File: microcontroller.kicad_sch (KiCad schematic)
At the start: 1 part, among them U1 STM32H745XIH6

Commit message: add power path sheet
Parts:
- U1: LCSC (none) -> C1338373
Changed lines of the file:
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@@
+			)
+		)
+		(property "LCSC" "C1338373"
+			(at 200.66 52.07 0)
+			(hide yes)
+			(show_name no)
+			(do_not_autoplace no)
+			(effects
+				(font
+					(size 1.27 1.27)
+				)
 			)
 		)
@@
 			)
 		)
+		(property "LCSC" "C1338373"
+			(at 59.69 100.33 0)
+			(hide yes)
+			(show_name no)
+			(do_not_autoplace no)
+			(effects
+				(font
+					(size 1.27 1.27)
+				)
+			)
+		)
 		(pin "D7"
 		)
@@
 			)
 		)
+		(property "LCSC" "C1338373"
+			(at 135.89 85.09 0)
+			(hide yes)
+			(show_name no)
+			(do_not_autoplace no)
+			(effects
+				(font
+					(size 1.27 1.27)
+				)
+			)
+		)

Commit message: fixed microcontroller footprint
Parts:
- U1: footprint STM32H745XIH6:BGA265C80P17X17_1400X1400X120 -> footprints:BGA265C80P17X17_1400X1400X120
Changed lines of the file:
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@@
 			)
 		)
-		(property "Footprint" "STM32H745XIH6:BGA265C80P17X17_1400X1400X120"
+		(property "Footprint" "footprints:BGA265C80P17X17_1400X1400X120"
 			(at 200.66 52.07 0)
 			(hide yes)
@@
 			)
 		)
-		(property "Footprint" "STM32H745XIH6:BGA265C80P17X17_1400X1400X120"
+		(property "Footprint" "footprints:BGA265C80P17X17_1400X1400X120"
 			(at 59.69 100.33 0)
 			(hide yes)
@@
 			)
 		)
-		(property "Footprint" "STM32H745XIH6:BGA265C80P17X17_1400X1400X120"
+		(property "Footprint" "footprints:BGA265C80P17X17_1400X1400X120"
 			(at 135.89 85.09 0)
 			(hide yes)

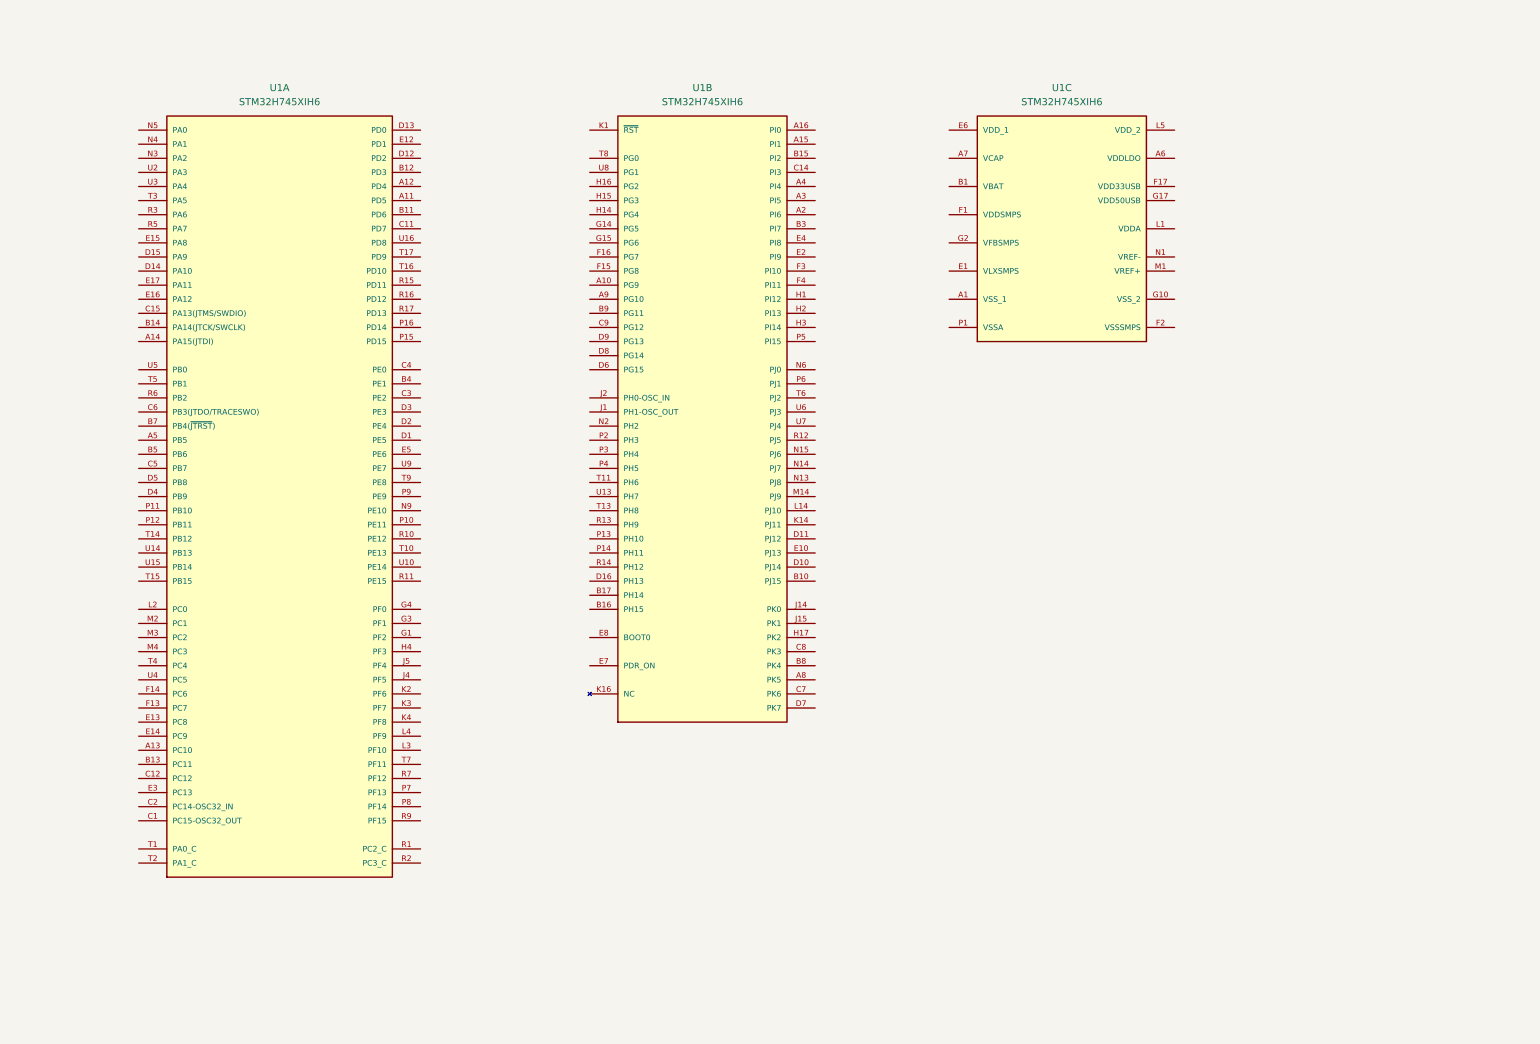
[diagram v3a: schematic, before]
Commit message: MCU (#2)
* add pedal cubemx file

* add microcontroller decoupling

* add decoupling caps

* fix footprints and add smps

* add user led

* add usb

* add debug pins

* add fmc pins, stomp uart, fuel gauge i2c

* update ioc

* add a bunch of peripherals

* add all external signals

* add no connects

* add oscillator
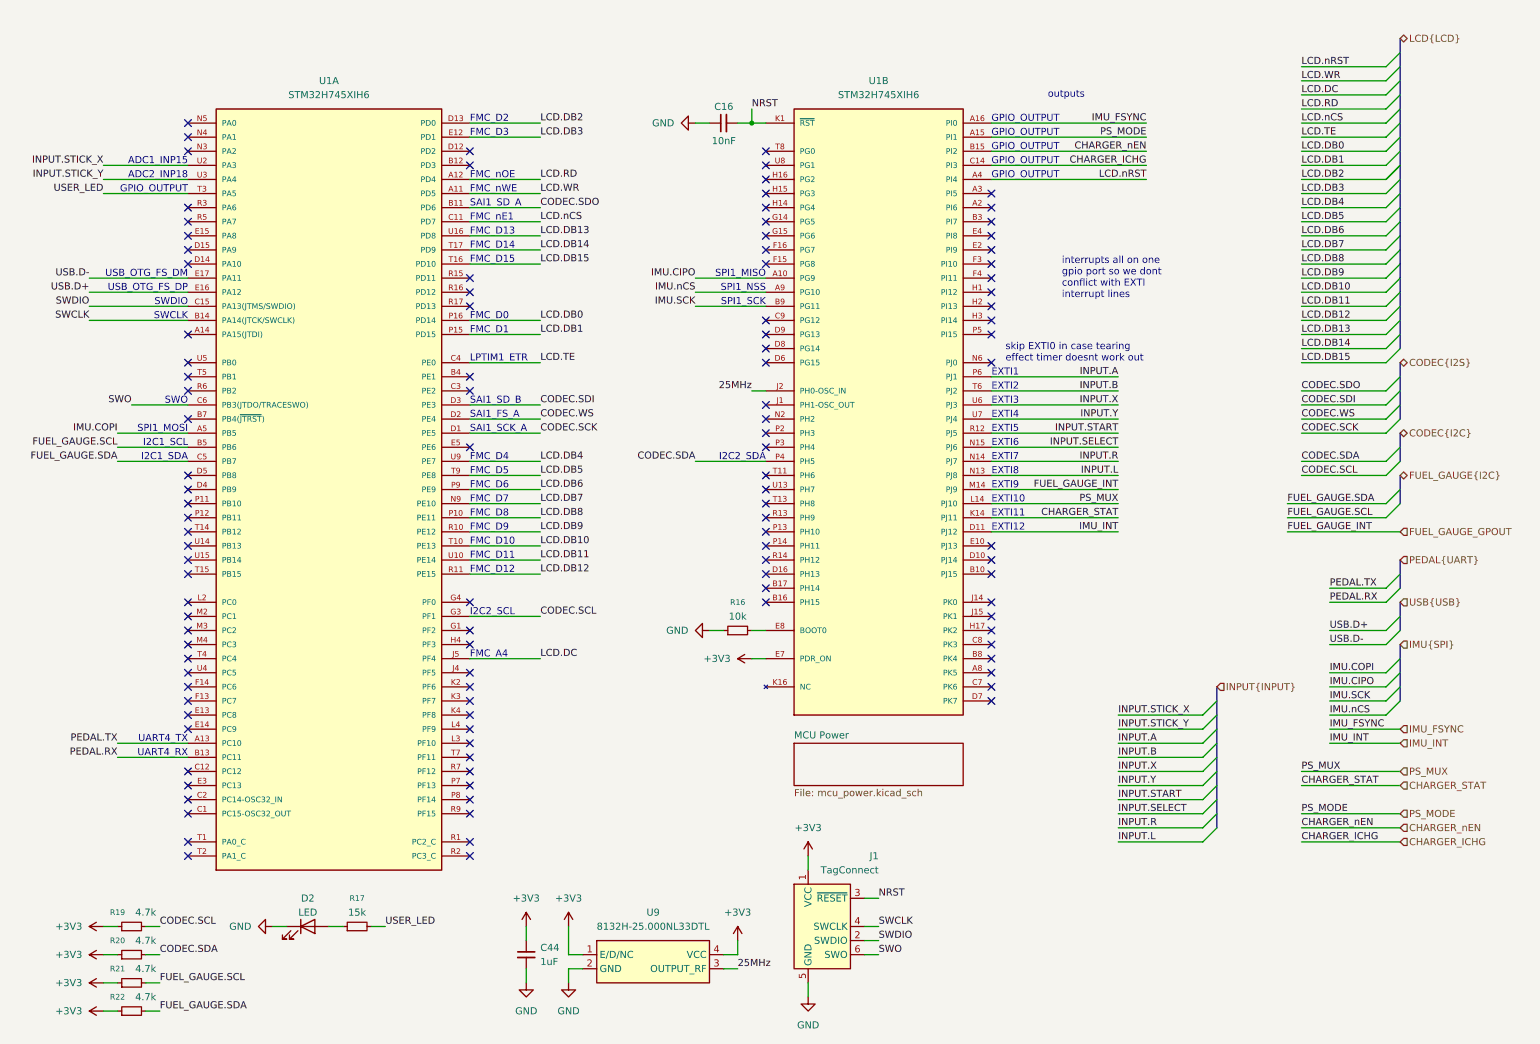
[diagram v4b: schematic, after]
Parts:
- removed unit 3 of U1
- added C16: 10nF, Capacitor_SMD:C_0402_1005Metric, symbol Device:C_Small
- added C44: 1uF, Capacitor_SMD:C_0402_1005Metric, symbol Device:C_Small
- added D2: LED, LED_SMD:LED_0402_1005Metric, symbol Device:LED
- added J1: TagConnect, Connector:Tag-Connect_TC2030-IDC-NL_2x03_P1.27mm_Vertical, symbol Connector:Conn_ARM_SWD_TagConnect_TC2030-NL
- added R16: 10k, Resistor_SMD:R_0402_1005Metric, symbol Device:R_Small
- added R17: 15k, Resistor_SMD:R_0402_1005Metric, symbol Device:R_Small
- added R19, R20, R21, R22: 4.7k, Resistor_SMD:R_0402_1005Metric, symbol Device:R_Small
- added U9: 8132H-25.000NL33DTL, custom:OSC-SMD_4P-L3.2-W2.5-BL, symbol custom:8132H-25.000NL33DTL
- U1: footprint footprints:BGA265C80P17X17_1400X1400X120 -> custom:BGA265C80P17X17_1400X1400X120
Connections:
- net LCD.WR: now reaches U1.A11 (PD5)
- net LCD.RD: now reaches U1.A12 (PD4)
- net PEDAL.TX: now reaches U1.A13 (PC10)
- net IMU.COPI: now reaches U1.A5 (PB5)
- net CODEC.SDO: now reaches U1.B11 (PD6)
- net PEDAL.RX: now reaches U1.B13 (PC11)
- net SWCLK: now reaches U1.B14 (PA14(JTCK/SWCLK))
- net SWCLK: now also J1.4 (SWCLK)
- net FUEL_GAUGE.SCL: now reaches U1.B5 (PB6)
- net FUEL_GAUGE.SCL: now also R21.2
- net LCD.nCS: now reaches U1.C11 (PD7)
- net SWDIO: now reaches U1.C15 (PA13(JTMS/SWDIO))
- net SWDIO: now also J1.2 (SWDIO)
- net LCD.TE: now reaches U1.C4 (PE0)
- net FUEL_GAUGE.SDA: now reaches U1.C5 (PB7)
- net FUEL_GAUGE.SDA: now also R22.2
- net SWO: now reaches U1.C6 (PB3(JTDO/TRACESWO))
- net SWO: now also J1.6 (SWO)
- net CODEC.SCK: now reaches U1.D1 (PE5)
- net LCD.DB2: now reaches U1.D13 (PD0)
- net CODEC.WS: now reaches U1.D2 (PE4)
- net CODEC.SDI: now reaches U1.D3 (PE3)
- net LCD.DB3: now reaches U1.E12 (PD1)
- net USB.D+: now reaches U1.E16 (PA12)
- net USB.D-: now reaches U1.E17 (PA11)
- net CODEC.SCL: now reaches U1.G3 (PF1)
- net CODEC.SCL: now also R19.2
- net LCD.DC: now reaches U1.J5 (PF4)
- net LCD.DB7: now reaches U1.N9 (PE10)
- net LCD.DB8: now reaches U1.P10 (PE11)
- net LCD.DB1: now reaches U1.P15 (PD15)
- net LCD.DB0: now reaches U1.P16 (PD14)
- net LCD.DB6: now reaches U1.P9 (PE9)
- net LCD.DB9: now reaches U1.R10 (PE12)
- net LCD.DB12: now reaches U1.R11 (PE15)
- net LCD.DB10: now reaches U1.T10 (PE13)
- net LCD.DB15: now reaches U1.T16 (PD10)
- net LCD.DB14: now reaches U1.T17 (PD9)
- net USER_LED: now reaches U1.T3 (PA5)
- net USER_LED: now also R17.2
- net LCD.DB5: now reaches U1.T9 (PE8)
- net LCD.DB11: now reaches U1.U10 (PE14)
- net LCD.DB13: now reaches U1.U16 (PD8)
- net INPUT.STICK_X: now reaches U1.U2 (PA3)
- net INPUT.STICK_Y: now reaches U1.U3 (PA4)
- net LCD.DB4: now reaches U1.U9 (PE7)
- net IMU.CIPO: now reaches U1.A10 (PG9)
- net PS_MODE: now reaches U1.A15 (PI1)
- net IMU_FSYNC: now reaches U1.A16 (PI0)
- net LCD.nRST: now reaches U1.A4 (PI4)
- net IMU.nCS: now reaches U1.A9 (PG10)
- net CHARGER_nEN: now reaches U1.B15 (PI2)
- net IMU.SCK: now reaches U1.B9 (PG11)
- net CHARGER_ICHG: now reaches U1.C14 (PI3)
- net IMU_INT: now reaches U1.D11 (PJ12)
- net +3V3: now reaches U1.E7 (PDR_ON)
- net +3V3: now also C44.1, J1.1 (VCC), R19.1, R20.1, R21.1, R22.1, U9.1 (E/D/NC), U9.4 (VCC)
- net at U1.E8 (BOOT0): now also R16.2
- net 25MHz: now reaches U1.J2 (PH0-OSC_IN)
- net 25MHz: now also U9.3 (OUTPUT_RF)
- net NRST: now reaches U1.K1 (~{RST})
- net NRST: now also C16.2, J1.3 (~{RESET})
- net CHARGER_STAT: now reaches U1.K14 (PJ11)
- net PS_MUX: now reaches U1.L14 (PJ10)
- net FUEL_GAUGE_GPOUT: now reaches U1.M14 (PJ9)
- net INPUT.L: now reaches U1.N13 (PJ8)
- net INPUT.R: now reaches U1.N14 (PJ7)
- net INPUT.SELECT: now reaches U1.N15 (PJ6)
- net CODEC.SDA: now reaches U1.P4 (PH5)
- net CODEC.SDA: now also R20.2
- net INPUT.A: now reaches U1.P6 (PJ1)
- net INPUT.START: now reaches U1.R12 (PJ5)
- net INPUT.B: now reaches U1.T6 (PJ2)
- net INPUT.X: now reaches U1.U6 (PJ3)
- net INPUT.Y: now reaches U1.U7 (PJ4)
- new net: D2.2 (A), R17.1
- new net GND: C16.1, C44.2, D2.1 (K), J1.5 (GND), R16.1, U9.2 (GND)
- no-connect marks 0 -> 111
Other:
- added sheet MCU Power (mcu_power.kicad_sch)
- note added: "ADC1_INP15"
- note added: "ADC2_INP18"
- note added: "EXTI1"
- note added: "EXTI10"
- note added: "EXTI11"
- note added: "EXTI12"
- note added: "EXTI2"
- note added: "EXTI3"
- note added: "EXTI4"
- note added: "EXTI5"
- note added: "EXTI6"
- note added: "EXTI7"
- note added: "EXTI8"
- note added: "EXTI9"
- note added: "FMC_A4"
- note added: "FMC_D0"
- note added: "FMC_D1"
- note added: "FMC_D10"
- note added: "FMC_D11"
- note added: "FMC_D12"
- note added: "FMC_D13"
- note added: "FMC_D14"
- note added: "FMC_D15"
- note added: "FMC_D2"
- note added: "FMC_D3"
- note added: "FMC_D4"
- note added: "FMC_D5"
- note added: "FMC_D6"
- note added: "FMC_D7"
- note added: "FMC_D8"
- note added: "FMC_D9"
- note added: "FMC_nE1"
- note added: "FMC_nOE"
- note added: "FMC_nWE"
- note added: "GPIO_OUTPUT"
- note added: "I2C1_SCL"
- note added: "I2C1_SDA"
- note added: "I2C2_SCL"
- note added: "I2C2_SDA"
- note added: "LPTIM1_ETR"
- note added: "SAI1_FS_A"
- note added: "SAI1_SCK_A"
- note added: "SAI1_SD_A"
- note added: "SAI1_SD_B"
- note added: "SPI1_MISO"
- note added: "SPI1_MOSI"
- note added: "SPI1_NSS"
- note added: "SPI1_SCK"
- note added: "SWCLK"
- note added: "SWDIO"
- note added: "SWO"
- note added: "UART4_RX"
- note added: "UART4_TX"
- note added: "USB_OTG_FS_DM"
- note added: "USB_OTG_FS_DP"
- note added: "interrupts all on one gpio port so we dont conflict with EXTI interrupt lines"
- note added: "outputs"
- note added: "skip EXTI0 in case tearing effect timer doesnt work out"
- moved on the sheet: U1A, U1B

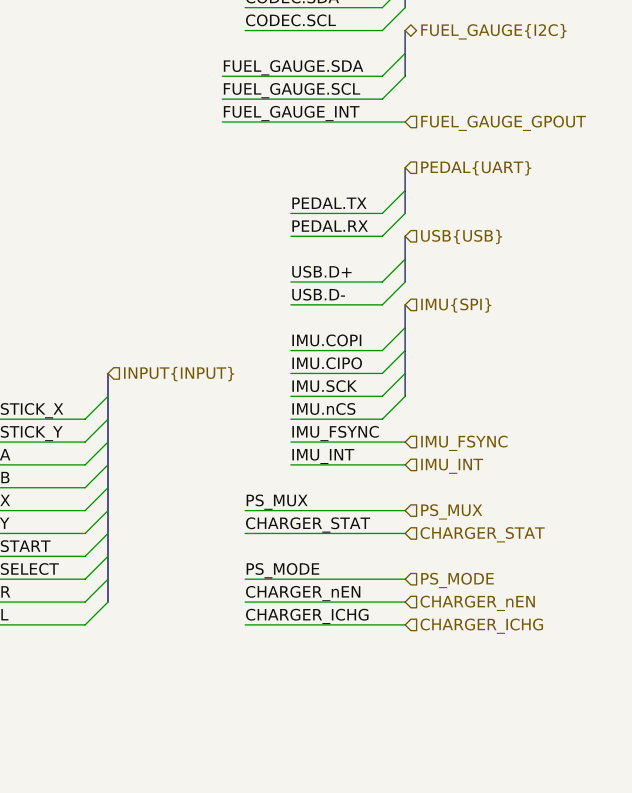
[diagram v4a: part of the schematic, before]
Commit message: IMU (#3)
* add imu sheet and library

* routing between sheets
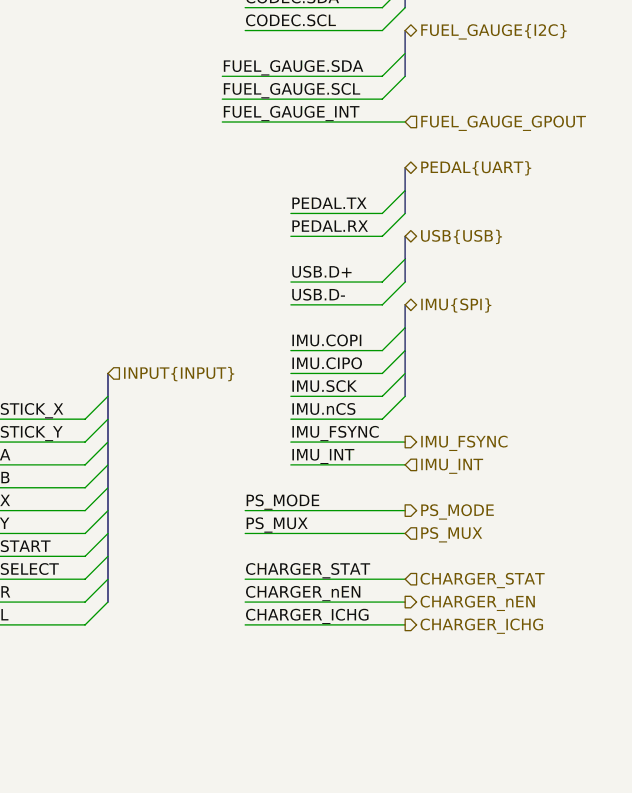
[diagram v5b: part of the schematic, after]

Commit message: add lcd backlight driver, hierarchical signals to display page
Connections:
- net BACKLIGHT_EN: now reaches U1.E15 (PA8)
- no-connect marks 111 -> 110
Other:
- note added: "TIM1_CH1"
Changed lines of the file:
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@@
 		)
 	)
+	(text "TIM1_CH1"
+		(exclude_from_sim no)
+		(at 43.18 53.34 0)
+		(effects
+			(font
+				(size 1.27 1.27)
+			)
+			(justify right bottom)
+		)
+	)
 	(text "skip EXTI0 in case tearing\neffect timer doesnt work out"
 		(exclude_from_sim no)
@@
 	)
 	(no_connect
-		(at 43.18 53.34)
-	)
-	(no_connect
 		(at 43.18 137.16)
 	)
@@
 	(wire
 		(pts
+			(xy 243.84 15.24) (xy 261.62 15.24)
+		)
+		(stroke
+			(width 0)
+			(type default)
+		)
+	)
+	(wire
+		(pts
 			(xy 243.84 149.86) (xy 261.62 149.86)
 		)
@@
 	(wire
 		(pts
+			(xy 27.94 53.34) (xy 43.18 53.34)
+		)
+		(stroke
+			(width 0)
+			(type default)
+		)
+	)
+	(wire
+		(pts
 			(xy 33.02 83.82) (xy 43.18 83.82)
 		)
@@
 		)
 	)
+	(label "BACKLIGHT_EN"
+		(at 243.84 15.24 0)
+		(effects
+			(font
+				(size 1.27 1.27)
+			)
+			(justify left bottom)
+		)
+	)
 	(label "SWO"
 		(at 33.02 83.82 180)
@@
 		)
 	)
+	(label "BACKLIGHT_EN"
+		(at 27.94 53.34 180)
+		(effects
+			(font
+				(size 1.27 1.27)
+			)
+			(justify right bottom)
+		)
+	)
 	(label "FUEL_GAUGE.SCL"
 		(at 241.3 104.14 0)
@@
 		(effects
 			(font
+				(size 1.27 1.27)
+			)
+			(justify left)
+		)
+	)
+	(hierarchical_label "BACKLIGHT_EN"
+		(shape output)
+		(at 261.62 15.24 0)
+		(effects
+			(font
